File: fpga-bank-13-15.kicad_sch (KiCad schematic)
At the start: 3 parts, among them U4 XC7K160T-FFG676

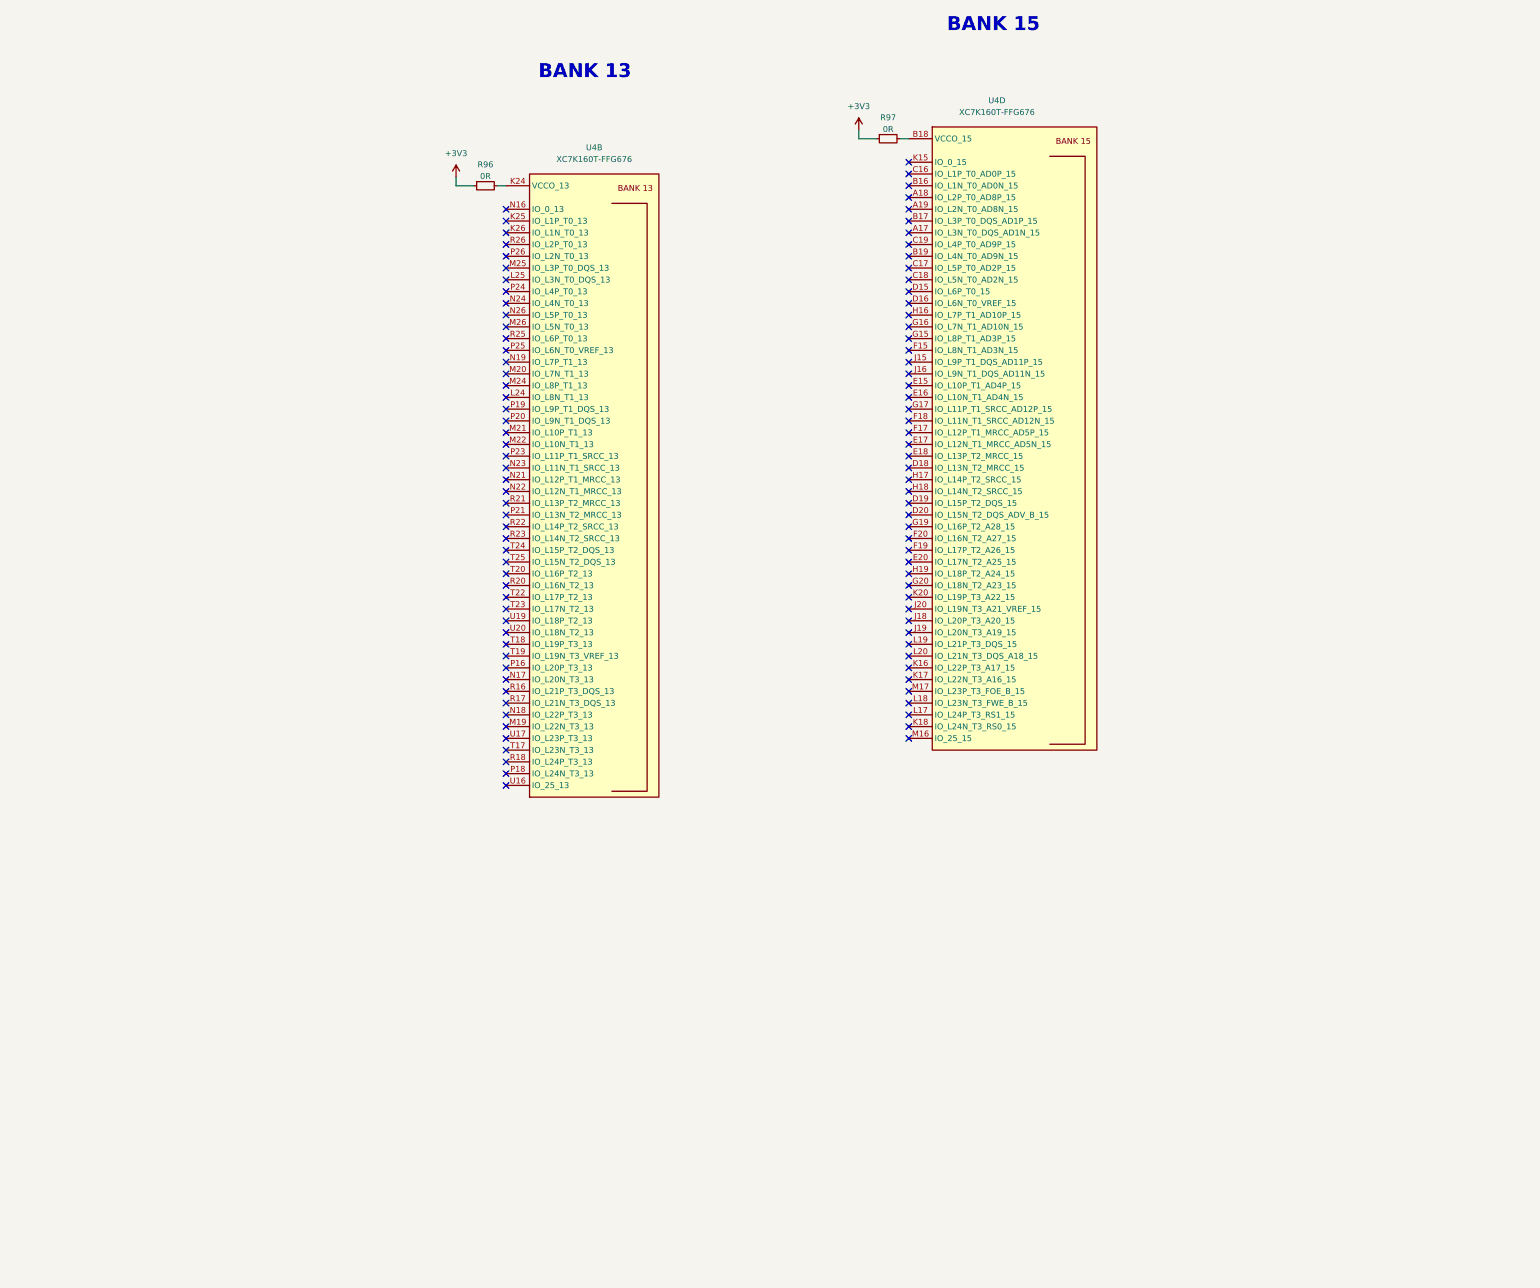
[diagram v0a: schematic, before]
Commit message: Finish reconnecting signals after migration to the hierarchical structure
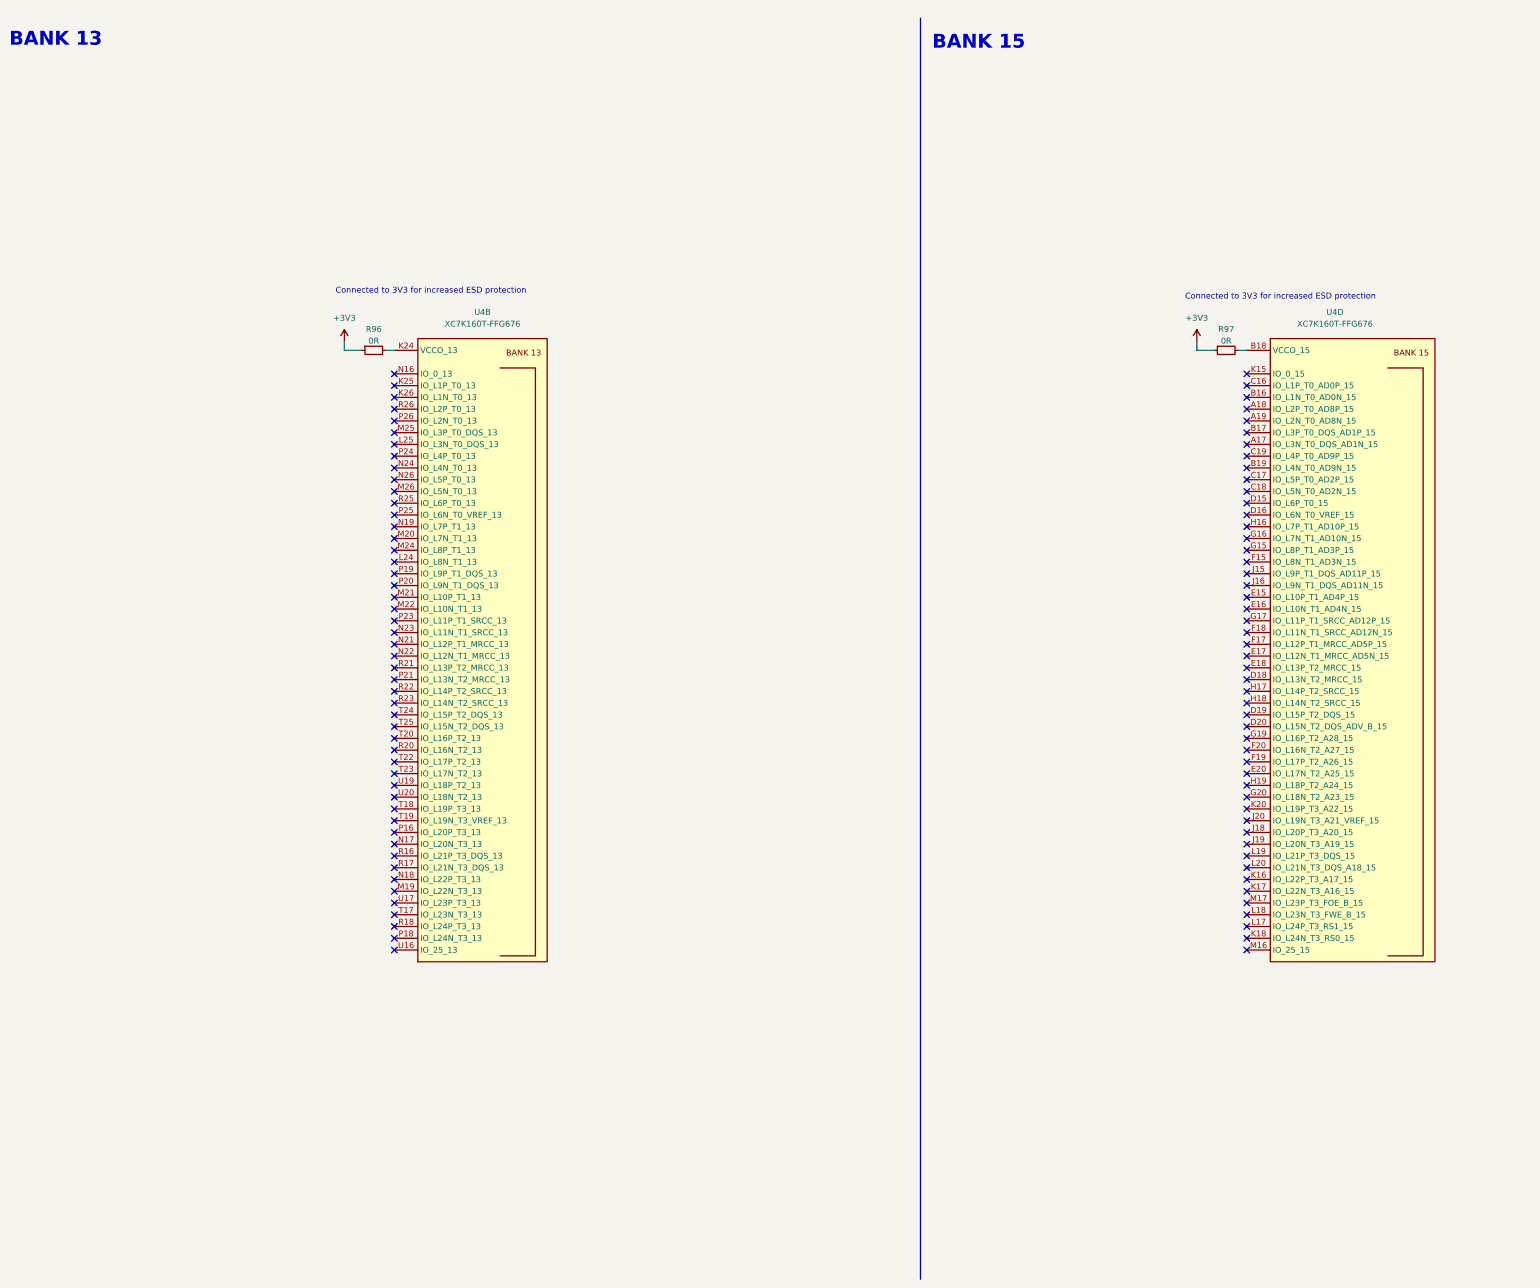
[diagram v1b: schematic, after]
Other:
- note added: "Connected to 3V3 for increased ESD protection"
- moved on the sheet: R96, R97, U4B, U4D

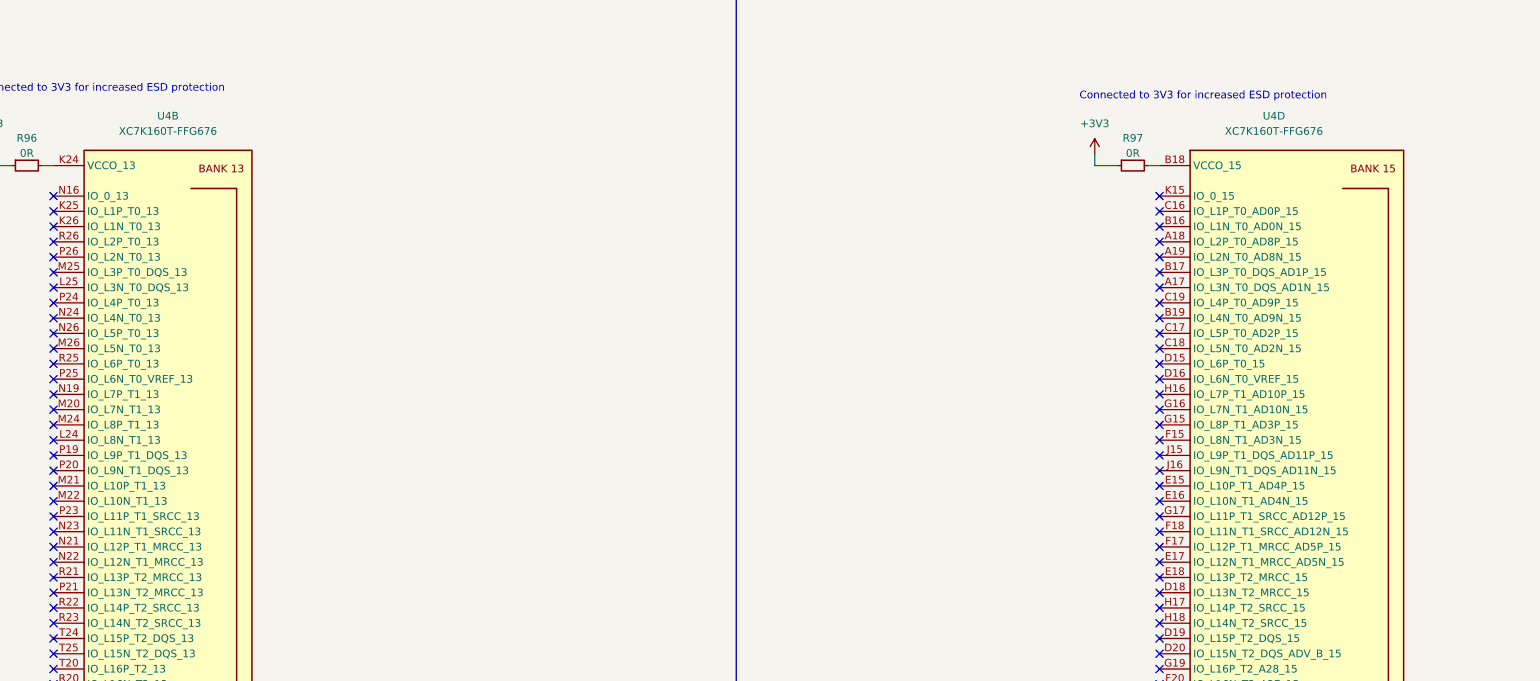
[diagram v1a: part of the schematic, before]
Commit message: Fix FPGA properties from the standardized library, update SO-DIMM symbol
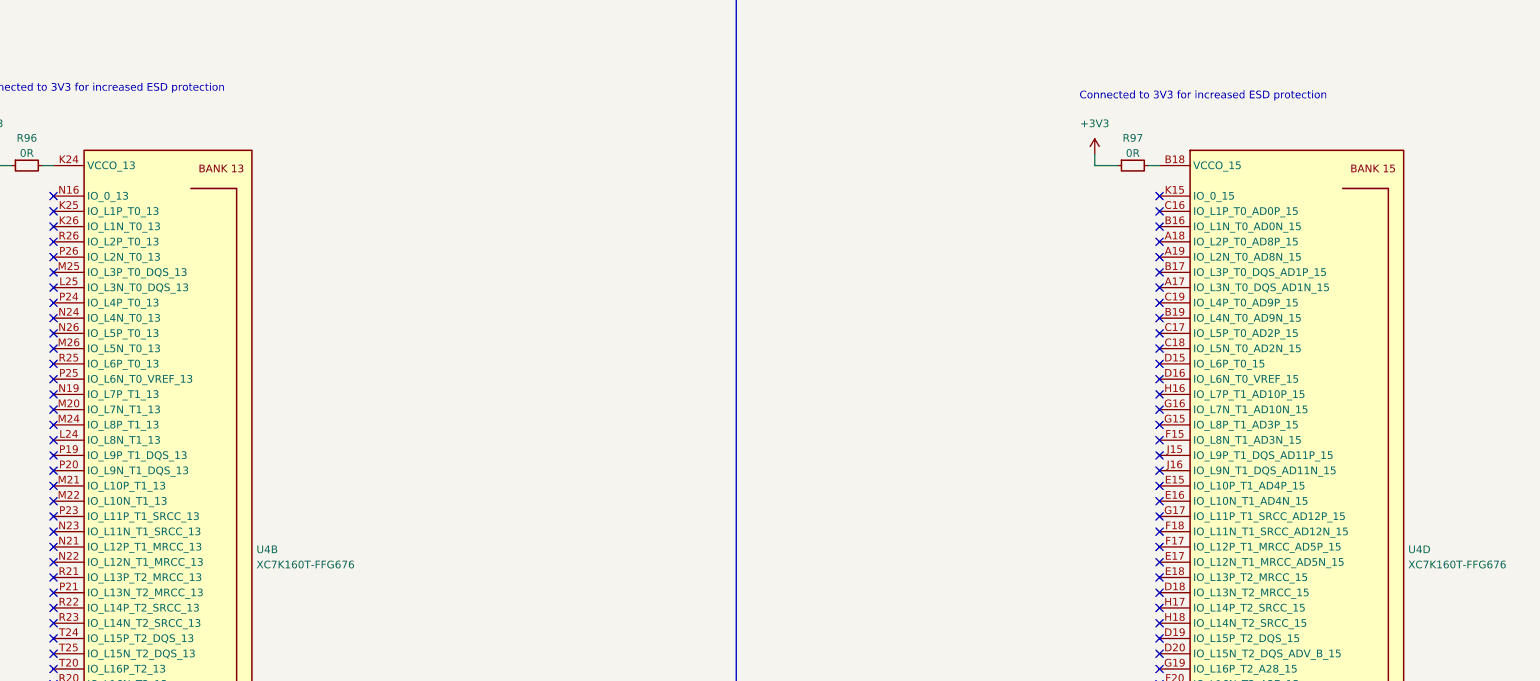
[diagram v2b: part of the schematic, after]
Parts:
- U4: footprint sodimm-ddr5-tester-footprints:BGA-676_27x27mm_Layout26x26_P1X1mm -> antmicro-footprints:BGA-676_27x27mm_Layout26x26_P1X1mm; symbol sodimm-ddr5-tester:XC7K160T-FFG676 -> antmicroMicrocontrollers:XC7K160T-FFG676; Manufacturer Xilinx -> AMD-Xilinx
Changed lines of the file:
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@@
     (effects (font (size 1.27 1.27)) (justify left bottom))
   )
-  (symbol (lib_id "sodimm-ddr5-tester:XC7K160T-FFG676") (at 280.67 83.82 0) (unit 4)
+  (symbol (lib_id "antmicroMicrocontrollers:XC7K160T-FFG676") (at 280.67 83.82 0) (unit 4)
     (in_bom yes) (on_board yes) (fields_autoplaced)
-    (property "Reference" "U4" (id 0) (at 299.72 75.565 0))
-    (property "Value" "XC7K160T-FFG676" (id 1) (at 299.72 78.105 0)
-      (effects (font (size 1.27 1.27) (thickness 0.15)))
-    )
-    (property "Footprint" "sodimm-ddr5-tester-footprints:BGA-676_27x27mm_Layout26x26_P1X1mm" (id 2) (at 349.25 86.36 0)
+    (property "Reference" "U4" (id 0) (at 322.072 147.7594 0)
+      (effects (font (size 1.27 1.27)) (justify left))
+    )
+    (property "Value" "XC7K160T-FFG676" (id 1) (at 322.072 150.2897 0)
+      (effects (font (size 1.27 1.27) (thickness 0.15)) (justify left))
+    )
+    (property "Footprint" "antmicro-footprints:BGA-676_27x27mm_Layout26x26_P1X1mm" (id 2) (at 349.25 86.36 0)
       (effects (font (size 1.27 1.27) (thickness 0.15)) (justify left bottom) hide)
     )
@@
       (effects (font (size 1.27 1.27) (thickness 0.15)) (justify left bottom) hide)
     )
-    (property "Manufacturer" "Xilinx" (id 7) (at 280.67 83.82 0)
+    (property "Manufacturer" "AMD-Xilinx" (id 7) (at 280.67 83.82 0)
       (effects (font (size 1.27 1.27)) hide)
     )
@@
     (pin "1")
   )
-  (symbol (lib_id "sodimm-ddr5-tester:XC7K160T-FFG676") (at 96.52 83.82 0) (unit 2)
+  (symbol (lib_id "antmicroMicrocontrollers:XC7K160T-FFG676") (at 96.52 83.82 0) (unit 2)
     (in_bom yes) (on_board yes) (fields_autoplaced)
-    (property "Reference" "U4" (id 0) (at 115.57 75.565 0))
-    (property "Value" "XC7K160T-FFG676" (id 1) (at 115.57 78.105 0)
-      (effects (font (size 1.27 1.27) (thickness 0.15)))
-    )
-    (property "Footprint" "sodimm-ddr5-tester-footprints:BGA-676_27x27mm_Layout26x26_P1X1mm" (id 2) (at 165.1 86.36 0)
+    (property "Reference" "U4" (id 0) (at 130.302 147.7594 0)
+      (effects (font (size 1.27 1.27)) (justify left))
+    )
+    (property "Value" "XC7K160T-FFG676" (id 1) (at 130.302 150.2897 0)
+      (effects (font (size 1.27 1.27) (thickness 0.15)) (justify left))
+    )
+    (property "Footprint" "antmicro-footprints:BGA-676_27x27mm_Layout26x26_P1X1mm" (id 2) (at 165.1 86.36 0)
       (effects (font (size 1.27 1.27) (thickness 0.15)) (justify left bottom) hide)
     )
@@
       (effects (font (size 1.27 1.27) (thickness 0.15)) (justify left bottom) hide)
     )
-    (property "Manufacturer" "Xilinx" (id 7) (at 96.52 83.82 0)
-      (effects (font (size 1.27 1.27)) hide)
-    )
+    (property "Manufacturer" "AMD-Xilinx" (id 7) (at 96.52 83.82 0)
+      (effects (font (size 1.27 1.27)) hide)
+    )

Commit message: Loclib of the project
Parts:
- U4: footprint antmicro-footprints:BGA-676_27x27mm_Layout26x26_P1X1mm -> sodimm-ddr5-tester-footprints:BGA-676_27x27mm_Layout26x26_P1X1mm; symbol antmicroMicrocontrollers:XC7K160T-FFG676 -> sodimm-ddr5-tester:XC7K160T-FFG676

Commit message: Clean schematic DRC
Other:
- moved on the sheet: R96, R97

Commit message: [#57478] ohp release
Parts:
- R96, R97: footprint sodimm-ddr5-tester-footprints:R_0402_1005Metric_EIA -> antmicro-footprints:R_0402_1005Metric; symbol sodimm-ddr5-tester:R_0R_0402 -> antmicroResistors0402:R_0R_0402
- U4: footprint sodimm-ddr5-tester-footprints:BGA-676_27x27mm_Layout26x26_P1X1mm -> antmicro-footprints:BGA-676_27x27mm_Layout26x26_P1x1mm_FFG676; symbol sodimm-ddr5-tester:XC7K160T-FFG676 -> antmicroFPGAChips:XC7K160T-FFG676
